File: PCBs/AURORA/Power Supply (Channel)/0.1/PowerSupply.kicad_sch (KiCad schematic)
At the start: 41 parts, among them J1 Conn_01x02_Male, J10 Conn_01x03_Male, J2 Conn_01x02_Male, J3 Conn_01x03_Male, J4 Conn_01x03_Male, J5 Conn_01x02_Pin, J6 Conn_01x02_Male, J7 Conn_01x02_Pin, J8 Conn_01x02_Male, U1 INA260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

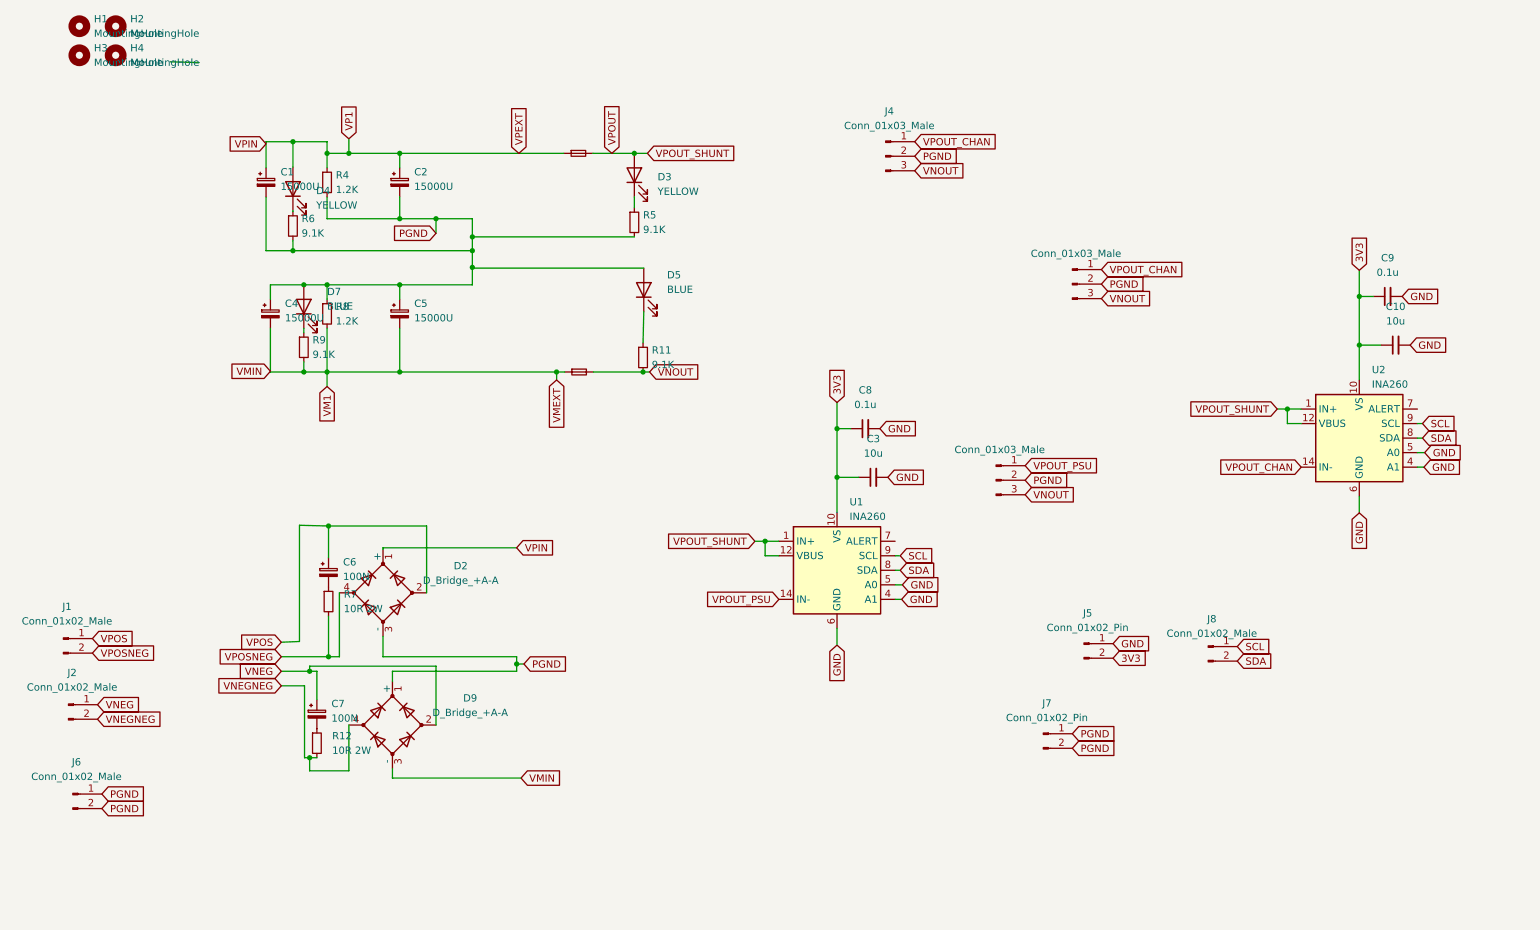
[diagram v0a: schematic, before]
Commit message: Fixing audio issues, leave TRUNC off and at 24 bits
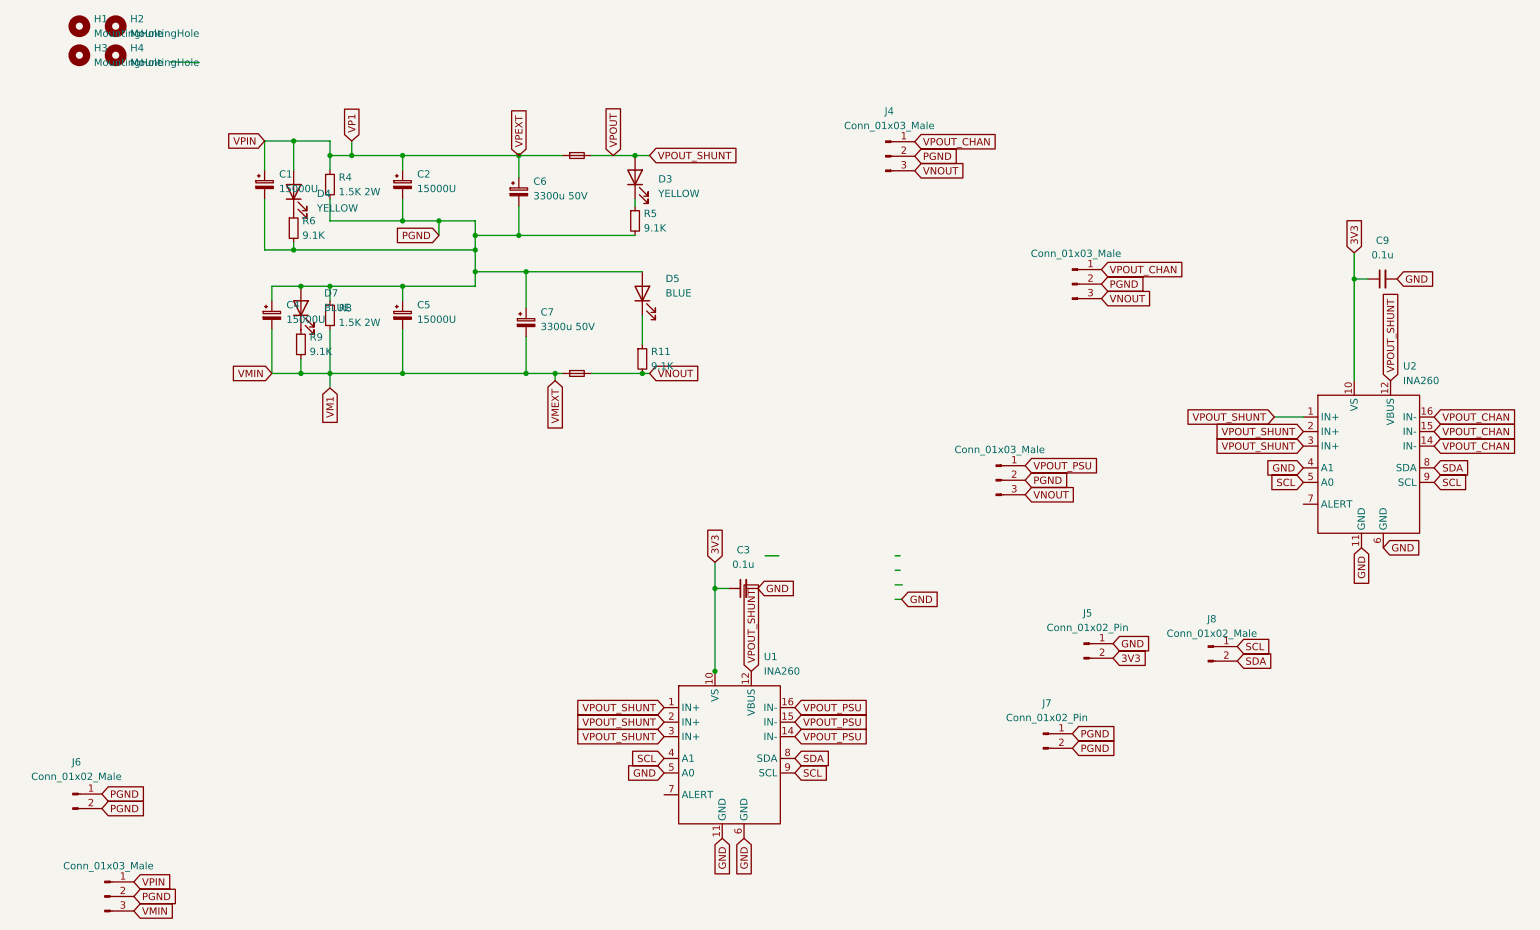
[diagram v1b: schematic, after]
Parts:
- removed C10: 10u, Capacitor_SMD:C_1206_3216Metric_Pad1.33x1.80mm_HandSolder, symbol Device:C_Small
- removed C8: 0.1u, Capacitor_SMD:C_0805_2012Metric_Pad1.18x1.45mm_HandSolder, symbol Device:C_Small
- removed D2, D9: D_Bridge_+A-A, Diode_SMD:Diode_Bridge_Vishay_DFS, symbol Device:D_Bridge_+A-A
- removed J1, J2: Conn_01x02_Male, Connector_JST:JST_VH_B2P-VH-B_1x02_P3.96mm_Vertical, symbol Connector:Conn_01x02_Male
- removed R12, R7: 10R 2W, Resistor_THT:R_Axial_DIN0411_L9.9mm_D3.6mm_P15.24mm_Horizontal, symbol Device:R_Small
- removed U1, U2: INA260, Package_SO:TSSOP-16_4.4x5mm_P0.65mm, symbol Sensor:INA260
- added J9: Conn_01x03_Male, Connector_JST:JST_VH_B3P-VH_1x03_P3.96mm_Vertical, symbol Connector:Conn_01x03_Male
- added U1, U2: INA260, Package_SO:TSSOP-16_4.4x5mm_P0.65mm, symbol Custom:INA260
- C3: value 10u -> 0.1u; footprint Capacitor_SMD:C_1206_3216Metric_Pad1.33x1.80mm_HandSolder -> Capacitor_SMD:C_0805_2012Metric_Pad1.18x1.45mm_HandSolder
- C6, C7: value 100N -> 3300u 50V; footprint Capacitor_THT:C_Rect_L13.0mm_W6.0mm_P10.00mm_FKS3_FKP3_MKS4 -> Capacitor_THT:CP_Radial_D18.0mm_P7.50mm
- R4, R8: value 1.2K -> 1.5K 2W; footprint Resistor_THT:R_Axial_DIN0414_L11.9mm_D4.5mm_P15.24mm_Horizontal -> Resistor_SMD:R_2512_6332Metric_Pad1.40x3.35mm_HandSolder
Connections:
- net VNEG is gone; now on net PGND: C7.1
- net VPOS is gone; now on net VP1: C6.1
- net 3V3: now also U1.10 (VS), U2.10 (VS)
- net GND: now also U1.11 (GND), U1.5 (A0), U1.6 (GND), U2.11 (GND), U2.4 (A1), U2.6 (GND)
- net PGND: now also C6.2, J9.2 (Pin_2)
- net SCL: now also U1.4 (A1), U1.9 (SCL), U2.5 (A0), U2.9 (SCL)
- net SDA: now also U1.8 (SDA), U2.8 (SDA)
- net VM1: now also C7.2, J9.3 (Pin_3)
- net VP1: now also J9.1 (Pin_1)
- net VPOUT: now also U1.1 (IN+), U1.12 (VBUS), U1.2 (IN+), U1.3 (IN+), U2.1 (IN+), U2.12 (VBUS), U2.2 (IN+), U2.3 (IN+)
- net VPOUT_CHAN: now also U2.14 (IN-), U2.15 (IN-), U2.16 (IN-)
- net VPOUT_PSU: now also U1.14 (IN-), U1.15 (IN-), U1.16 (IN-)
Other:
- moved on the sheet: C2, C5, C9, D4, D5, D7, R4, R8, R9
